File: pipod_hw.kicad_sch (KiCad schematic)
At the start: 2 parts

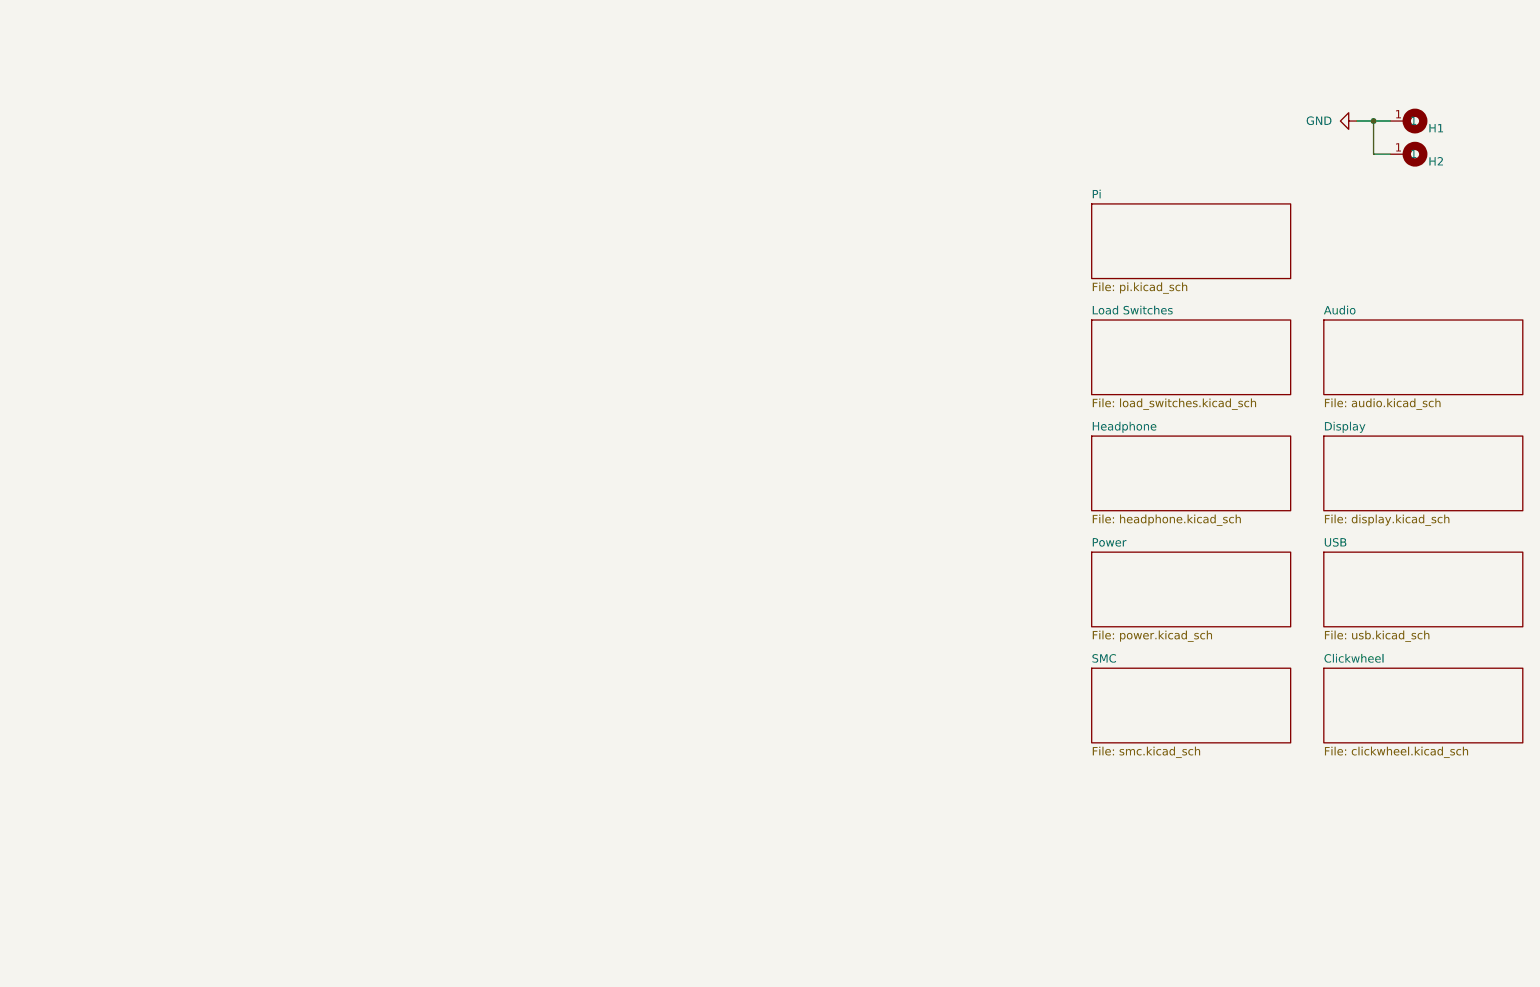
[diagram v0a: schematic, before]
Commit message: layout: add testpoints, extra mounting hole, grounding clips
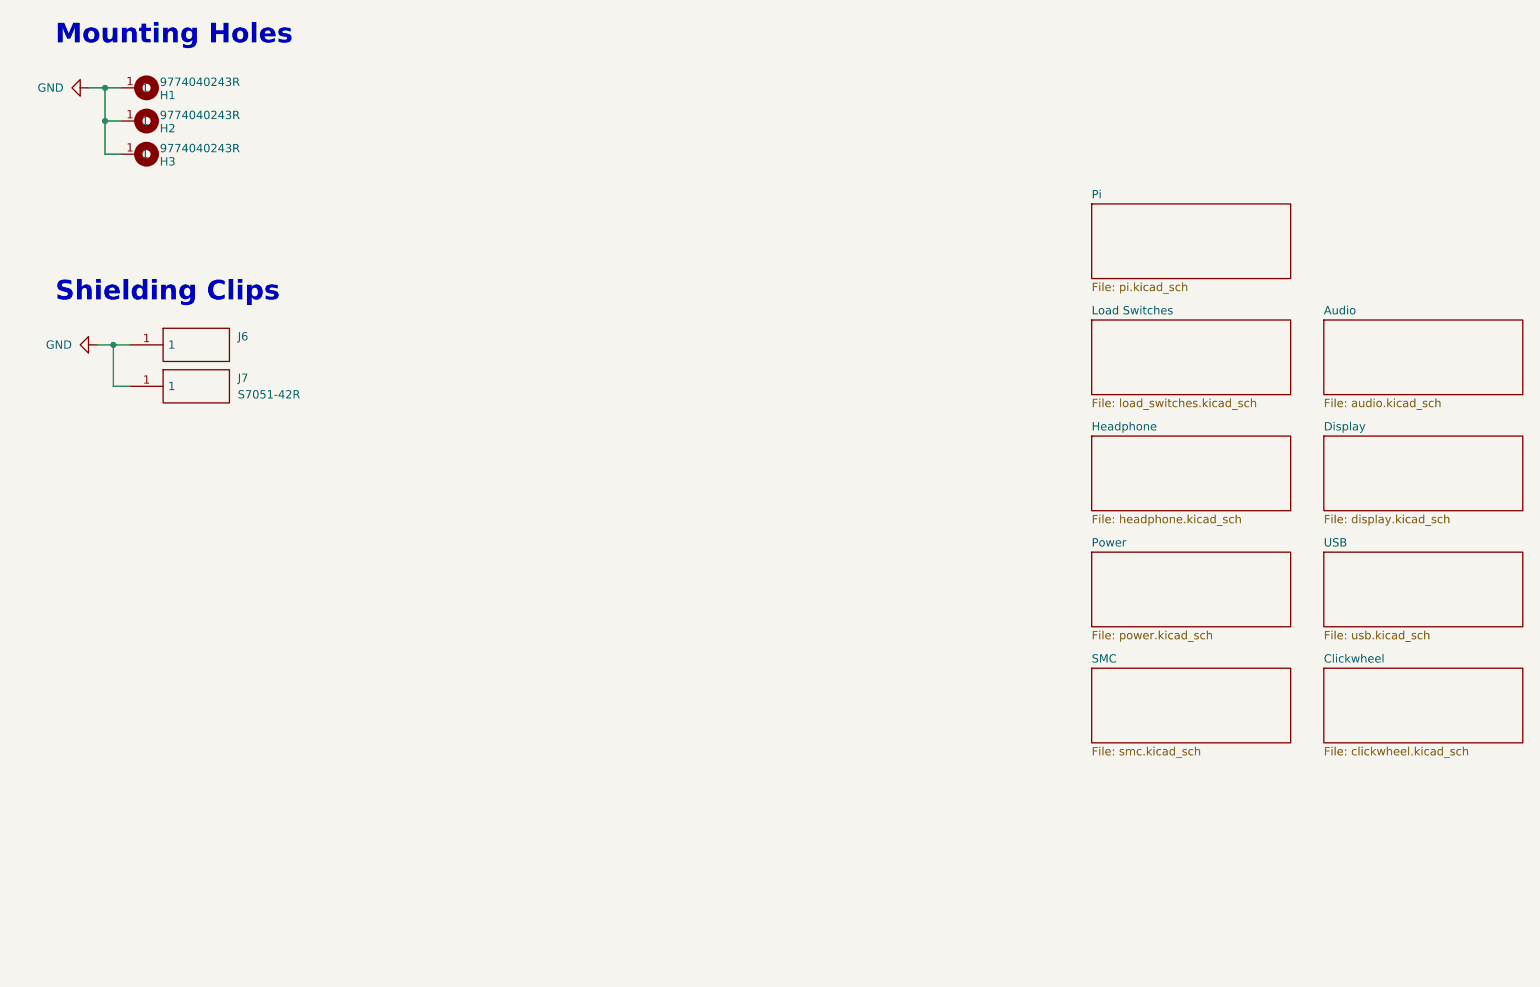
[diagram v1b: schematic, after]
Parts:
- added H3: 9774040243R, Gigahawk:9774040243R, symbol gigahawk:9774040243R
- added J6: (no value), symbol gigahawk:S7051-42R
- added J7: S7051-42R, Gigahawk:S705142R, symbol gigahawk:S7051-42R
- H1, H2: value (none) -> 9774040243R; footprint (none) -> Gigahawk:9774040243R
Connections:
- net GND: now also H3.1, J6.1, J7.1
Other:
- note added: "Mounting Holes"
- note added: "Shielding Clips"
- moved on the sheet: H1, H2

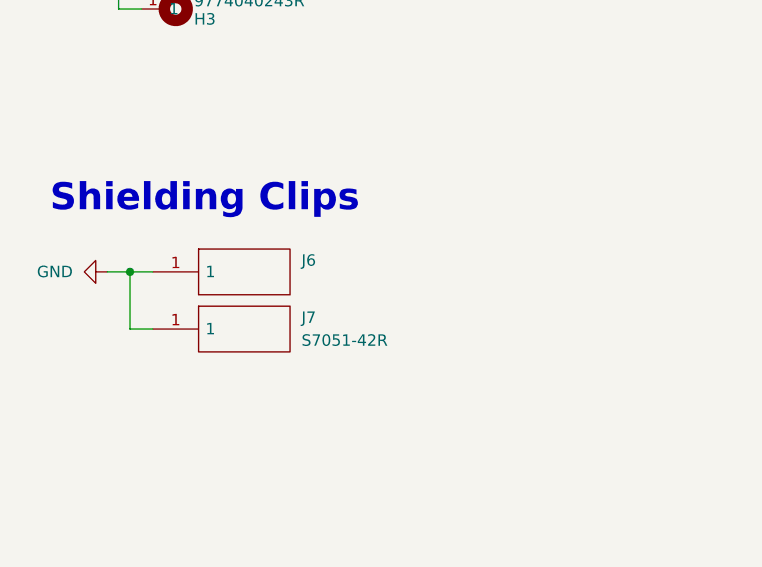
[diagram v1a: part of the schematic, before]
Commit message: layout: cleanup silkscreen, add bootloader buttons
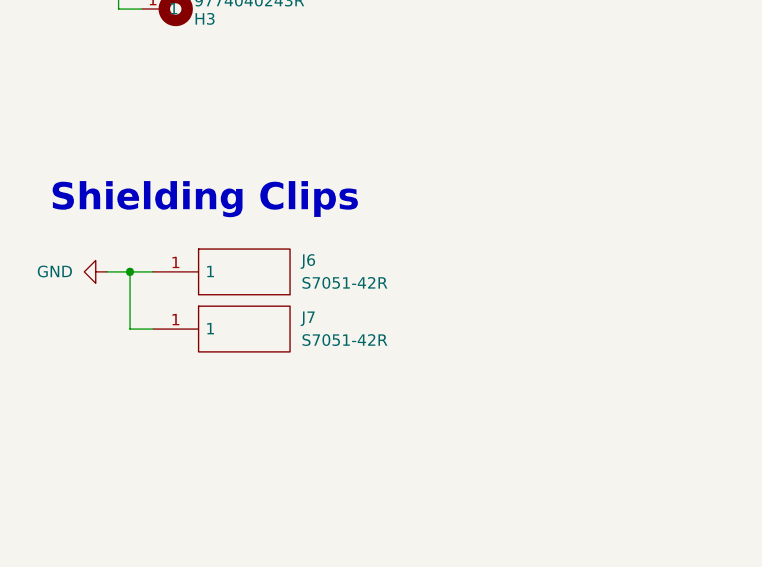
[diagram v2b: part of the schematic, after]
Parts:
- J6: value (none) -> S7051-42R; footprint (none) -> Gigahawk:S705142R
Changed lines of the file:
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@@
       (effects (font (size 1.27 1.27)) (justify left))
     )
-    (property "Value" "" (id 1) (at 58.42 83.8199 0)
+    (property "Value" "S7051-42R" (id 1) (at 58.42 83.8199 0)
       (effects (font (size 1.27 1.27)) (justify left))
     )
-    (property "Footprint" "" (id 2) (at 58.42 80.01 0)
+    (property "Footprint" "Gigahawk:S705142R" (id 2) (at 58.42 80.01 0)
       (effects (font (size 1.27 1.27)) (justify left) hide)
     )
@@
       (reference "#PWR0141") (unit 1) (value "GND") (footprint "")
     )
+    (path "/f4aab422-c542-43e3-8476-eae6a2df1847/c4ed1f25-8011-4f17-b9b7-a4903f46d522"
+      (reference "#PWR0142") (unit 1) (value "GND") (footprint "")
+    )
+    (path "/f4aab422-c542-43e3-8476-eae6a2df1847/f0226c4c-3d26-444f-b8c4-b9528f9282f3"
+      (reference "#PWR0143") (unit 1) (value "GND") (footprint "")
+    )
     (path "/9641055c-ce4b-4f2f-881f-d2622ca62ef8/e768d9dc-f7c9-45e3-99e1-a1498a2ff958"
       (reference "C1") (unit 1) (value "100n") (footprint "Capacitor_SMD:C_0402_1005Metric")
@@
     )
     (path "/f4aab422-c542-43e3-8476-eae6a2df1847/0a3de141-38e2-4729-972e-41552c2c892a"
-      (reference "R12") (unit 1) (value "10k") (footprint "Resistor_SMD:R_0402_1005Metric")
+      (reference "R12") (unit 1) (value "1k") (footprint "Resistor_SMD:R_0402_1005Metric")
     )
     (path "/f4aab422-c542-43e3-8476-eae6a2df1847/75e0d85d-82be-411b-99af-60d91d3d58e7"
-      (reference "R13") (unit 1) (value "DNP") (footprint "Resistor_SMD:R_0402_1005Metric")
+      (reference "R13") (unit 1) (value "10k") (footprint "Resistor_SMD:R_0402_1005Metric")
     )
     (path "/f4aab422-c542-43e3-8476-eae6a2df1847/bafa32ec-a838-4599-8bed-936054011aef"
@@
       (reference "R47") (unit 1) (value "10k") (footprint "Resistor_SMD:R_0402_1005Metric")
     )
+    (path "/f4aab422-c542-43e3-8476-eae6a2df1847/bc88214e-07aa-453d-a4d6-d40e0ac901ec"
+      (reference "SW1") (unit 1) (value "SW_Push") (footprint "Gigahawk:SW_Push_1P1T_NO_CK_KMR2")
+    )
+    (path "/f4aab422-c542-43e3-8476-eae6a2df1847/c2e7fc5a-7e19-4013-9cc0-20f3b3210d10"
+      (reference "SW2") (unit 1) (value "SW_Push") (footprint "Gigahawk:SW_Push_1P1T_NO_CK_KMR2")
+    )
     (path "/f4aab422-c542-43e3-8476-eae6a2df1847/dc354bb6-7b51-4421-92e0-ea2af5ff7fbb"

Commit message: ci: prepare files for CI
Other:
- title: (none) -> piPod IO/SMC Board
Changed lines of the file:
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@@
 (kicad_sch (version 20211123) (generator eeschema)
   (paper "A4")
+  (title_block
+    (title "piPod IO/SMC Board")
+    (date "${DATE}")
+    (rev "%{TAG} (${REVISION})")
+  )
   (junction (at 38.1 43.18) (diameter 0) (color 0 0 0 0)
   )
@@
     )
     (path "/9641055c-ce4b-4f2f-881f-d2622ca62ef8/e2753e1f-594c-47fc-9a68-ae587552bc7e"
-      (reference "L1") (unit 1) (value "1u") (footprint "Inductor_SMD:L_Vishay_IFSC-1515AH_4x4x1.8mm")
+      (reference "L1") (unit 1) (value "1u") (footprint "Gigahawk:L_Vishay_IFSC-1515AH_4x4x1.8mm")
     )
     (path "/9641055c-ce4b-4f2f-881f-d2622ca62ef8/5722c5c4-8626-446d-9666-d9813f74a54f"
@@
     )
     (path "/eadbe3e2-ad3f-4ca7-9baa-62c6cdfbb2dc/0487b507-c9a1-41bc-859b-2c8e3fe6b107"
-      (reference "Q2") (unit 1) (value "NTK3139PT1G") (footprint "Package_TO_SOT_SMD:SOT-723")
+      (reference "Q2") (unit 1) (value "NTK3139PT1G") (footprint "Gigahawk:SOT-723")
     )
     (path "/1b9367eb-6062-4145-acac-45f8e2b4ead5/c3a6728c-dacb-445c-9f4d-b321b21cbd2e"
@@
     )
     (path "/9641055c-ce4b-4f2f-881f-d2622ca62ef8/f712dca8-d825-42b9-bc64-c896c523d0a2"
-      (reference "U1") (unit 1) (value "MAX17048G+T10") (footprint "Package_DFN_QFN:DFN-8-1EP_2x2mm_P0.5mm_EP0.6x1.2mm")
+      (reference "U1") (unit 1) (value "MAX17048G+T10") (footprint "Gigahawk:DFN-8-1EP_2x2mm_P0.5mm_EP0.6x1.2mm")
     )
     (path "/9641055c-ce4b-4f2f-881f-d2622ca62ef8/ab8b469c-69ca-4be9-a595-0f9e9bfbc4ba"
-      (reference "U2") (unit 1) (value "MAX8903AETI+T") (footprint "Package_DFN_QFN:QFN-28-1EP_4x4mm_P0.4mm_EP2.6x2.6mm")
+      (reference "U2") (unit 1) (value "MAX8903AETI+T") (footprint "Gigahawk:QFN-28-1EP_4x4mm_P0.4mm_EP2.6x2.6mm")
     )
     (path "/9641055c-ce4b-4f2f-881f-d2622ca62ef8/9364adad-fb7b-44df-8a98-69b3dbbbb081"
@@
     )
     (path "/f4aab422-c542-43e3-8476-eae6a2df1847/a1cd96cb-1cf2-42af-8049-9350ef4d78e3"
-      (reference "U5") (unit 1) (value "W25Q128JVS") (footprint "Package_SON:WSON-8-1EP_6x5mm_P1.27mm_EP3.4x4.3mm")
+      (reference "U5") (unit 1) (value "W25Q128JVS") (footprint "Gigahawk:WSON-8-1EP_6x5mm_P1.27mm_EP3.4x4.3mm")
     )
     (path "/f4aab422-c542-43e3-8476-eae6a2df1847/ec102973-8c1e-44ac-b5ab-fa9e9ce69d0a"
@@
     )
     (path "/1b9367eb-6062-4145-acac-45f8e2b4ead5/0808eb40-03d1-411a-82f9-5b336472169f"
-      (reference "U8") (unit 1) (value "RS2299XTQC16") (footprint "Package_DFN_QFN:QFN-16-1EP_3x3mm_P0.5mm_EP1.7x1.7mm")
+      (reference "U8") (unit 1) (value "RS2299XTQC16") (footprint "Gigahawk:QFN-16-1EP_3x3mm_P0.5mm_EP1.7x1.7mm")
     )
     (path "/17277ecf-326c-453e-9136-7d67138ec3e0/c8169392-03f0-4aa3-91e4-e02ade2584f2"
@@
     )
     (path "/47c80a0b-4e54-4420-855d-26a9531e4652/1c663c89-7f7d-47bf-9f9e-bb09a858cbfa"
-      (reference "U14") (unit 1) (value "PAM8908JER") (footprint "Package_DFN_QFN:QFN-16-1EP_3x3mm_P0.5mm_EP1.7x1.7mm")
+      (reference "U14") (unit 1) (value "PAM8908JER") (footprint "Gigahawk:QFN-16-1EP_3x3mm_P0.5mm_EP1.7x1.7mm")
     )
     (path "/b0bb8e22-3ad5-4c36-b10d-7d4a51e22334/2d1b5162-5ef3-4603-8719-3fe186178dd4"
-      (reference "U15") (unit 1) (value "MCP23008-E/ML") (footprint "Package_DFN_QFN:QFN-20-1EP_4x4mm_P0.5mm_EP2.7x2.7mm")
+      (reference "U15") (unit 1) (value "MCP23008-E/ML") (footprint "Gigahawk:QFN-20-1EP_4x4mm_P0.5mm_EP2.7x2.7mm")
     )
     (path "/f4aab422-c542-43e3-8476-eae6a2df1847/a57c84b5-5d55-414c-b5d7-cf18bbcbc814"
-      (reference "Y1") (unit 1) (value "12MHz 20pF") (footprint "Crystal:Crystal_SMD_2520-4Pin_2.5x2.0mm")
-    )
-  )
+      (reference "Y1") (unit 1) (value "12MHz 20pF") (footprint "Gigahawk:Crystal_SMD_2520-4Pin_2.5x2.0mm")
+    )
+  )

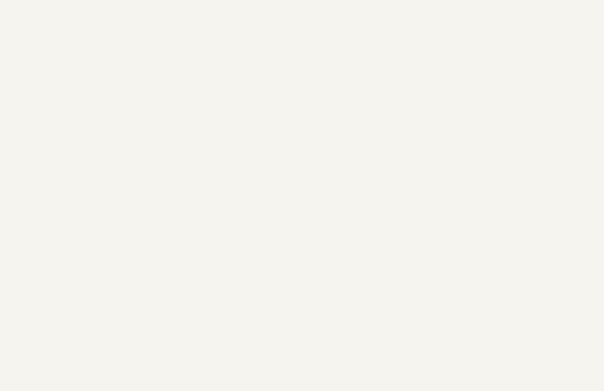
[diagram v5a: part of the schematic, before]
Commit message: layout: add OSHW logo, change version text to masked copper
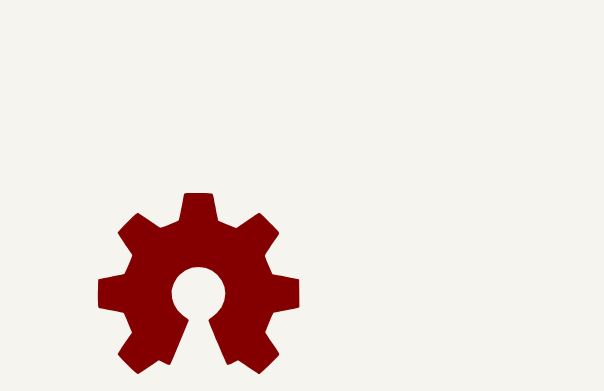
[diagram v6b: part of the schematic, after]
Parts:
- added LOGO1: (no value), symbol Graphic:Logo_Open_Hardware_Large
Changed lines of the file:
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@@
     (pin "1")
+  )
+  (symbol (lib_id "Graphic:Logo_Open_Hardware_Large") (at 46.99 170.18 0) (unit 1)
+    (in_bom yes) (on_board yes) (fields_autoplaced)
+    (property "Reference" "LOGO1" (id 0) (at 46.99 157.48 0)
+      (effects (font (size 1.27 1.27)) hide)
+    )
+    (property "Value" "" (id 1) (at 46.99 180.34 0)
+      (effects (font (size 1.27 1.27)) hide)
+    )
+    (property "Footprint" "" (id 2) (at 46.99 170.18 0)
+      (effects (font (size 1.27 1.27)) hide)
+    )
+    (property "Datasheet" "~" (id 3) (at 46.99 170.18 0)
+      (effects (font (size 1.27 1.27)) hide)
+    )
   )
   (sheet (at 189.23 78.74) (size 30.48 11.43) (fields_autoplaced)
@@
       (reference "L1") (unit 1) (value "1u") (footprint "Gigahawk:L_Vishay_IFSC-1515AH_4x4x1.8mm")
     )
+    (path "/f9ed3b68-da82-4cc1-82ff-dd13ba5666dc"
+      (reference "LOGO1") (unit 1) (value "Logo_Open_Hardware_Large") (footprint "Gigahawk:OSHW-Logo2_9.8x8mm_Mask")
+    )
     (path "/9641055c-ce4b-4f2f-881f-d2622ca62ef8/5722c5c4-8626-446d-9666-d9813f74a54f"

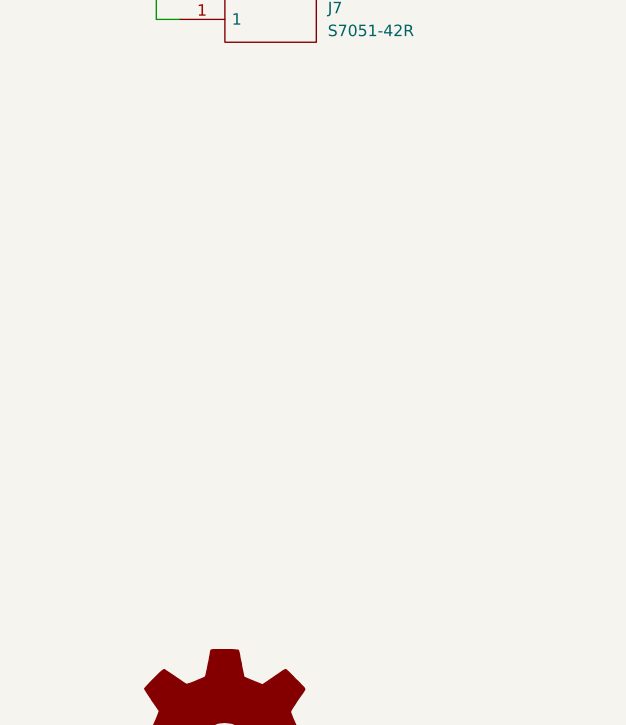
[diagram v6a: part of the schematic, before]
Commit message: feature: add hardware ID resistors
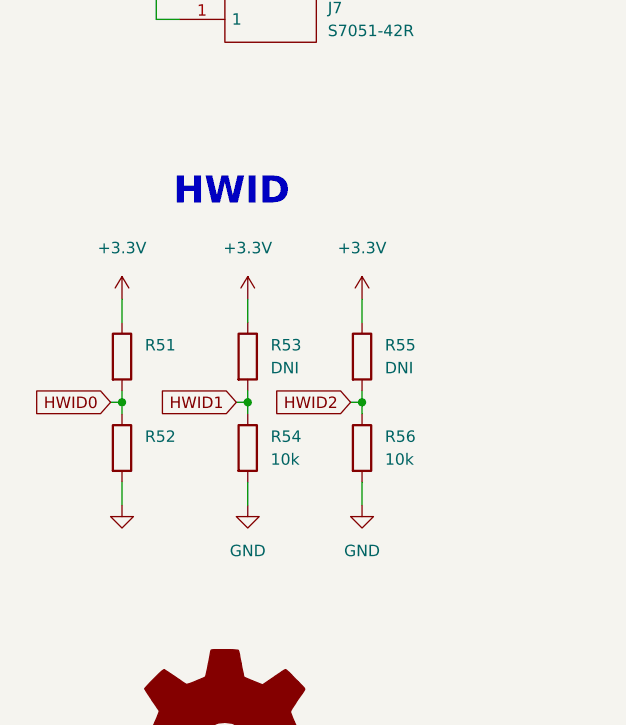
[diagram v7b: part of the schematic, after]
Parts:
- added R51: (no value), Resistor_SMD:R_0402_1005Metric, symbol Device:R
- added R52: (no value), symbol Device:R
- added R53, R55: DNI, Resistor_SMD:R_0402_1005Metric, symbol Device:R
- added R54, R56: 10k, Resistor_SMD:R_0402_1005Metric, symbol Device:R
- LOGO1: value (none) -> Logo_Open_Hardware_Large; footprint (none) -> Gigahawk:OSHW-Logo2_9.8x8mm_Mask
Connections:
- net GND: now also R52.2, R54.2, R56.2
- new net +3V3: R51.1, R53.1, R55.1
- new net HWID0: R51.2, R52.1
- new net HWID1: R53.2, R54.1
- new net HWID2: R55.2, R56.1
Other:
- note added: "HWID"
